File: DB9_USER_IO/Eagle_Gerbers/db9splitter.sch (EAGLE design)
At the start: 17 parts, among them IC1 74LVC1G04DBV

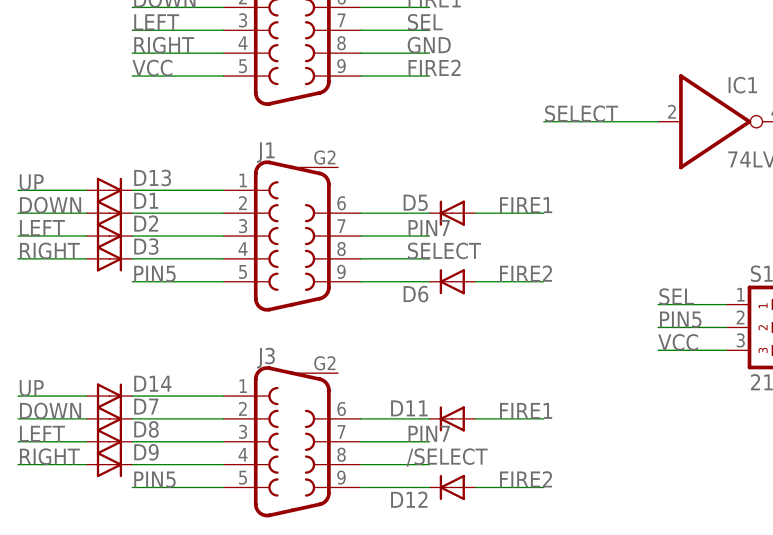
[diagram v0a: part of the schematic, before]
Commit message: Change splitter by 74HC157 circuit
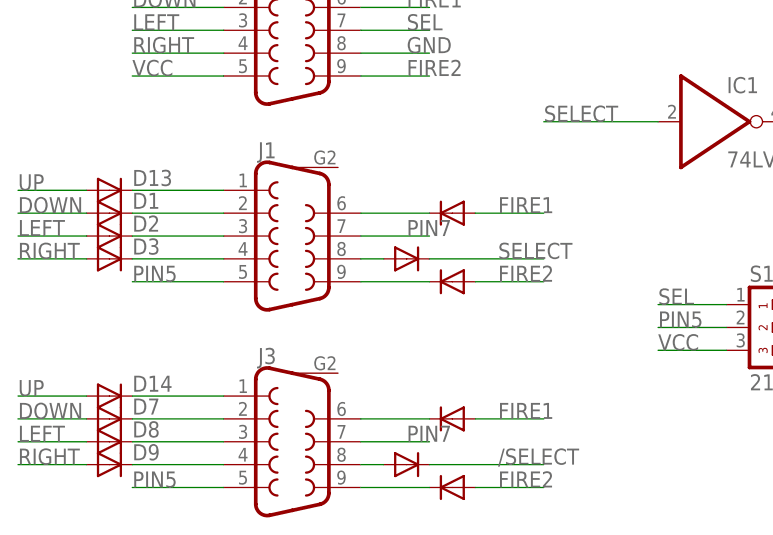
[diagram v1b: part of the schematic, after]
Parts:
- added D10, D4: (no value), diode:DIODE-SOD323-R
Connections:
- new net N$15: D4.A, J1.8
- new net N$9: D10.A, J3.8
- net /SELECT: now also D10.C; no longer J3.8
- net SELECT: now also D4.C; no longer J1.8
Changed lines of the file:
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@@
 <part name="D14" library="diode" deviceset="DIODE-" device="SOD323-R"/>
 <part name="S1" library="switch-dil" deviceset="219-03*" device="J" value="219-03J"/>
+<part name="D4" library="diode" deviceset="DIODE-" device="SOD323-R"/>
+<part name="D10" library="diode" deviceset="DIODE-" device="SOD323-R"/>
 </parts>
 <sheets>
@@
 <instances>
 <instance part="IC1" gate="A" x="45.72" y="96.52"/>
-<instance part="D1" gate="G$1" x="-20.32" y="86.36"/>
-<instance part="D2" gate="G$1" x="-20.32" y="83.82"/>
-<instance part="D3" gate="G$1" x="-20.32" y="81.28"/>
+<instance part="D1" gate="G$1" x="-20.32" y="86.36" smashed="yes">
+<attribute name="NAME" x="-17.78" y="86.8426" size="1.778" layer="95"/>
+<attribute name="VALUE" x="-17.78" y="84.0486" size="1.778" layer="96"/>
+</instance>
+<instance part="D2" gate="G$1" x="-20.32" y="83.82" smashed="yes">
+<attribute name="NAME" x="-17.78" y="84.3026" size="1.778" layer="95"/>
+<attribute name="VALUE" x="-17.78" y="81.5086" size="1.778" layer="96"/>
+</instance>
+<instance part="D3" gate="G$1" x="-20.32" y="81.28" smashed="yes">
+<attribute name="NAME" x="-17.78" y="81.7626" size="1.778" layer="95"/>
+<attribute name="VALUE" x="-17.78" y="78.9686" size="1.778" layer="96"/>
+</instance>
 <instance part="D5" gate="G$1" x="17.78" y="86.36" smashed="yes" rot="R180">
-<attribute name="NAME" x="15.24" y="88.4174" size="1.778" layer="95" rot="R180"/>
 <attribute name="VALUE" x="15.24" y="88.6714" size="1.778" layer="96" rot="R180"/>
 </instance>
-<instance part="D6" gate="G$1" x="17.78" y="78.74" rot="R180"/>
-<instance part="D7" gate="G$1" x="-20.32" y="63.5"/>
-<instance part="D8" gate="G$1" x="-20.32" y="60.96"/>
-<instance part="D9" gate="G$1" x="-20.32" y="58.42"/>
+<instance part="D6" gate="G$1" x="17.78" y="78.74" smashed="yes" rot="R180">
+<attribute name="VALUE" x="15.24" y="81.0514" size="1.778" layer="96" rot="R180"/>
+</instance>
+<instance part="D7" gate="G$1" x="-20.32" y="63.5" smashed="yes">
+<attribute name="NAME" x="-17.78" y="63.9826" size="1.778" layer="95"/>
+<attribute name="VALUE" x="-17.78" y="61.1886" size="1.778" layer="96"/>
+</instance>
+<instance part="D8" gate="G$1" x="-20.32" y="60.96" smashed="yes">
+<attribute name="NAME" x="-17.78" y="61.4426" size="1.778" layer="95"/>
+<attribute name="VALUE" x="-17.78" y="58.6486" size="1.778" layer="96"/>
+</instance>
+<instance part="D9" gate="G$1" x="-20.32" y="58.42" smashed="yes">
+<attribute name="NAME" x="-17.78" y="58.9026" size="1.778" layer="95"/>
+<attribute name="VALUE" x="-17.78" y="56.1086" size="1.778" layer="96"/>
+</instance>
 <instance part="D11" gate="G$1" x="17.78" y="63.5" smashed="yes" rot="R180">
-<attribute name="NAME" x="15.24" y="65.5574" size="1.778" layer="95" rot="R180"/>
 <attribute name="VALUE" x="15.24" y="65.8114" size="1.778" layer="96" rot="R180"/>
 </instance>
-<instance part="D12" gate="G$1" x="17.78" y="55.88" rot="R180"/>
+<instance part="D12" gate="G$1" x="17.78" y="55.88" smashed="yes" rot="R180">
+<attribute name="VALUE" x="15.24" y="58.1914" size="1.778" layer="96" rot="R180"/>
+</instance>
 <instance part="J2" gate="G$1" x="0" y="106.68"/>
 <instance part="J3" gate="G$1" x="0" y="60.96"/>
 <instance part="J1" gate="G$1" x="0" y="83.82"/>
-<instance part="D13" gate="G$1" x="-20.32" y="88.9"/>
-<instance part="D14" gate="G$1" x="-20.32" y="66.04"/>
+<instance part="D13" gate="G$1" x="-20.32" y="88.9" smashed="yes">
+<attribute name="NAME" x="-17.78" y="89.3826" size="1.778" layer="95"/>
+<attribute name="VALUE" x="-17.78" y="86.5886" size="1.778" layer="96"/>
+</instance>
+<instance part="D14" gate="G$1" x="-20.32" y="66.04" smashed="yes">
+<attribute name="NAME" x="-17.78" y="66.5226" size="1.778" layer="95"/>
+<attribute name="VALUE" x="-17.78" y="63.7286" size="1.778" layer="96"/>
+</instance>
 <instance part="S1" gate="G$1" x="55.88" y="73.66" rot="R270"/>
+<instance part="D4" gate="G$1" x="12.7" y="81.28" smashed="yes">
+<attribute name="VALUE" x="15.24" y="78.9686" size="1.778" layer="96"/>
+</instance>
+<instance part="D10" gate="G$1" x="12.7" y="58.42" smashed="yes">
+<attribute name="VALUE" x="15.24" y="56.1086" size="1.778" layer="96"/>
+</instance>
 </instances>
 <busses>
@@
 </segment>
 <segment>
-<wire x1="7.62" y1="81.28" x2="15.24" y2="81.28" width="0.1524" layer="91"/>
-<label x="12.7" y="81.28" size="1.778" layer="95"/>
-<pinref part="J1" gate="G$1" pin="8"/>
-</segment>
-<segment>
 <pinref part="J2" gate="G$1" pin="P$1"/>
 <wire x1="5.08" y1="116.84" x2="15.24" y2="116.84" width="0.1524" layer="91"/>
 <label x="12.7" y="116.84" size="1.778" layer="95"/>
 </segment>
+<segment>
+<pinref part="D4" gate="G$1" pin="C"/>
+<wire x1="15.24" y1="81.28" x2="27.94" y2="81.28" width="0.1524" layer="91"/>
+<label x="22.86" y="81.28" size="1.778" layer="95"/>
+</segment>
 </net>
 <net name="/SELECT" class="0">
@@
 </segment>
 <segment>
-<wire x1="7.62" y1="58.42" x2="15.24" y2="58.42" width="0.1524" layer="91"/>
-<label x="12.7" y="58.42" size="1.778" layer="95"/>
-<pinref part="J3" gate="G$1" pin="8"/>
+<pinref part="D10" gate="G$1" pin="C"/>
+<wire x1="15.24" y1="58.42" x2="27.94" y2="58.42" width="0.1524" layer="91"/>
+<label x="22.86" y="58.42" size="1.778" layer="95"/>
 </segment>
 </net>
@@
 </segment>
 </net>
+<net name="N$9" class="0">
+<segment>
+<pinref part="J3" gate="G$1" pin="8"/>
+<pinref part="D10" gate="G$1" pin="A"/>
+<wire x1="10.16" y1="58.42" x2="7.62" y2="58.42" width="0.1524" layer="91"/>
+</segment>
+</net>
+<net name="N$15" class="0">
+<segment>
+<pinref part="J1" gate="G$1" pin="8"/>
+<pinref part="D4" gate="G$1" pin="A"/>
+<wire x1="7.62" y1="81.28" x2="10.16" y2="81.28" width="0.1524" layer="91"/>
+</segment>
+</net>

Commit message: updated db9splitter
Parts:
- removed D1, D10, D11, D12, D13, D14, D2, D3, D4, D5, D6, D7, D8, D9: (no value), diode:DIODE-SOD323-R
- removed IC1: 74LVC1G04DBV, 74xx-little-de:74LVC1G04DBV
- added IC2, IC3: 74HC157D, 74xx-eu:74HC157D
- added RN2, RN3, RN5: 10K, resistor-dil:4R-N0603-ARC
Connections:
- removed net /SELECT: D10.C, IC1A.O
- removed net N$1: D13.C, J1.1
- removed net N$11: D6.C, J1.9
- removed net N$12: D5.C, J1.6
- removed net N$13: D12.C, J3.9
- removed net N$14: D11.C, J3.6
- removed net N$15: D4.A, J1.8
- removed net N$2: D14.C, J3.1
- removed net N$3: D2.C, J1.3
- removed net N$4: D8.C, J3.3
- removed net N$5: D1.C, J1.2
- removed net N$6: D3.C, J1.4
- removed net N$7: D7.C, J3.2
- removed net N$8: D9.C, J3.4
- removed net N$9: D10.A, J3.8
- new net 1PDOWN: IC2A.4A, J1.2, RN2A.1
- new net 1PFIRE1: IC3A.3A, J1.6, RN5A.1
- new net 1PFIRE2: IC3A.2A, J1.9, RN5C.1
- new net 1PLEFT: IC2A.2A, J1.3, RN5B.1
- new net 1PRIGHT: IC2A.1A, J1.4, RN5D.1
- new net 1PUP: IC2A.3A, J1.1, RN2B.1
- new net 2PDOWN: IC2A.4B, J3.2, RN3A.1
- new net 2PFIRE1: IC3A.3B, J3.6, RN2D.1
- new net 2PFIRE2: IC3A.2B, J3.9, RN3D.1
- new net 2PLEFT: IC2A.2B, J3.3, RN3B.1
- new net 2PRIGHT: IC2A.1B, J3.4, RN3C.1
- new net 2PUP: IC2A.3B, J3.1, RN2C.1
- net DOWN: now also IC2A.4Y; no longer D1.A, D7.A
- net FIRE1: now also IC3A.3Y; no longer D11.A, D5.A
- net FIRE2: now also IC3A.2Y; no longer D12.A, D6.A
- net GND: now also IC2A.G, IC3A.G, J1.8, J3.8
- net LEFT: now also IC2A.2Y; no longer D2.A, D8.A
- net RIGHT: now also IC2A.1Y; no longer D3.A, D9.A
- net SELECT: now also IC2A.!A!/B, IC3A.!A!/B; no longer D4.C, IC1A.I
- net UP: now also IC2A.3Y; no longer D13.A, D14.A
- net VCC: now also RN2A.2, RN2B.2, RN2C.2, RN2D.2, RN3A.2, RN3B.2, RN3C.2, RN3D.2, RN5A.2, RN5B.2, RN5C.2, RN5D.2
